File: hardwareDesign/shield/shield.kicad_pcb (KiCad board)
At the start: 2 copper layers, 71 parts, among them J10 PIM_LCD, J11 WQP419, J12 WQP419, J2 40_POS_Header, J3 WQP419, J4 10_POS_PIN_HEADER_ALT, J5 WQP419, J6 WQP419, J7 WQP419, J8 WQP419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

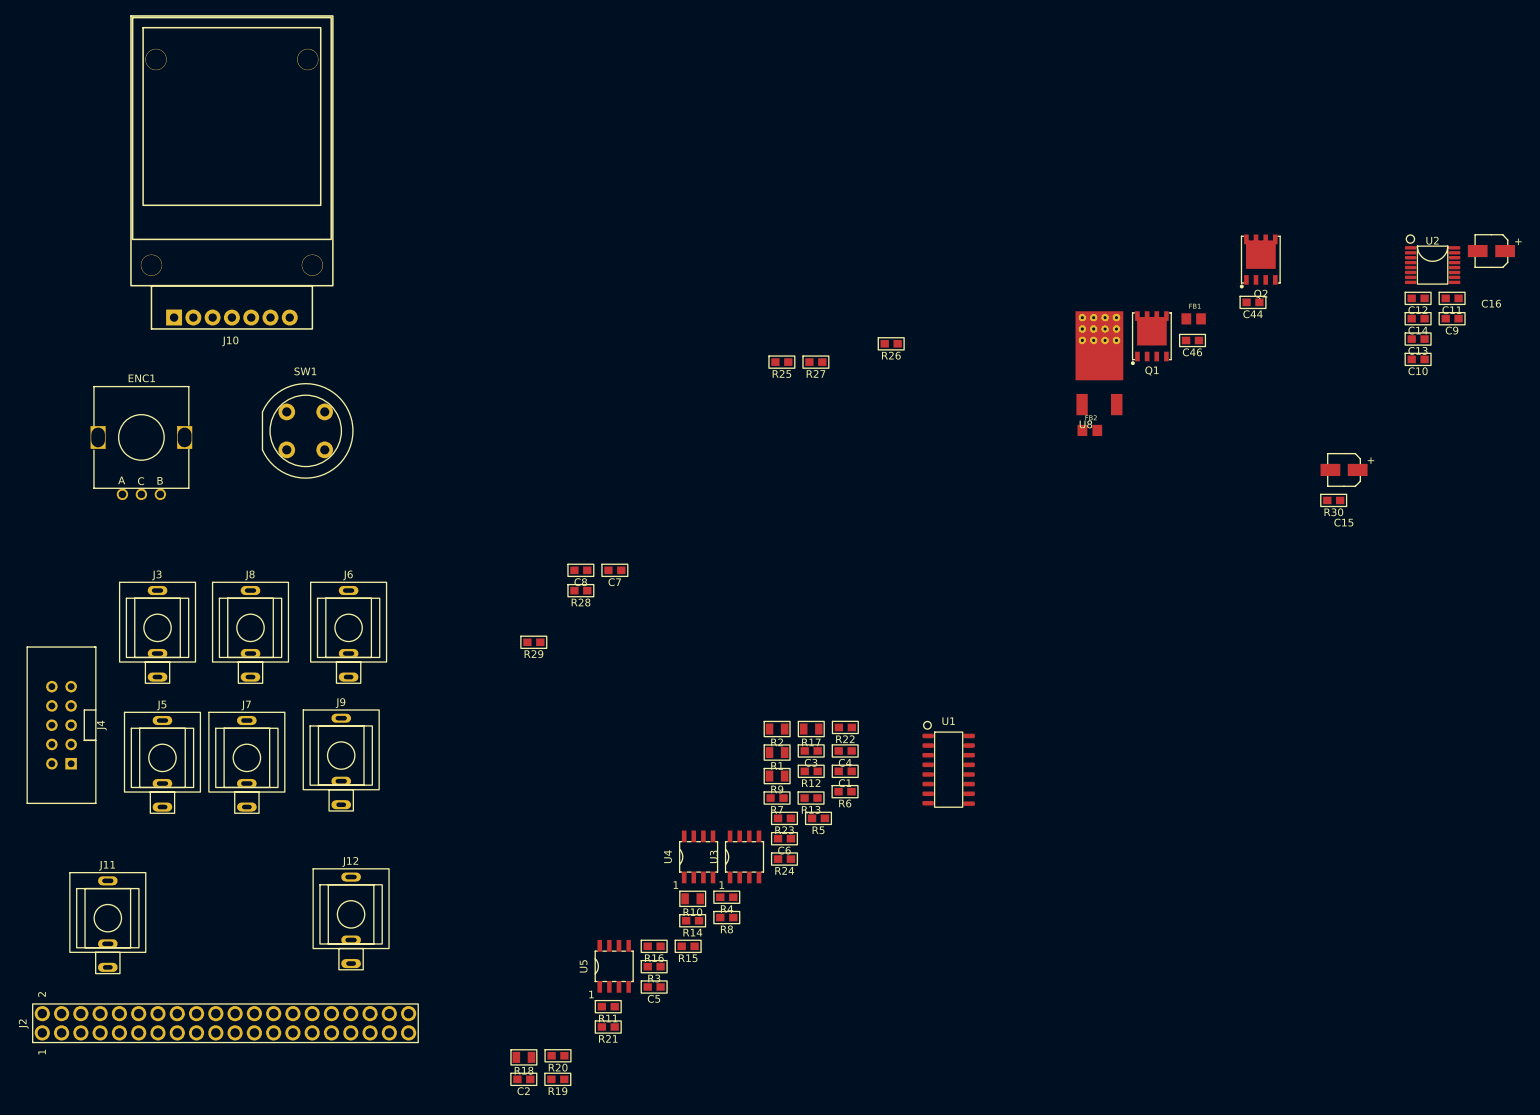
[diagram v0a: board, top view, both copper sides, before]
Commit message: Finished schematic and PCB for jetson Nano Sheild
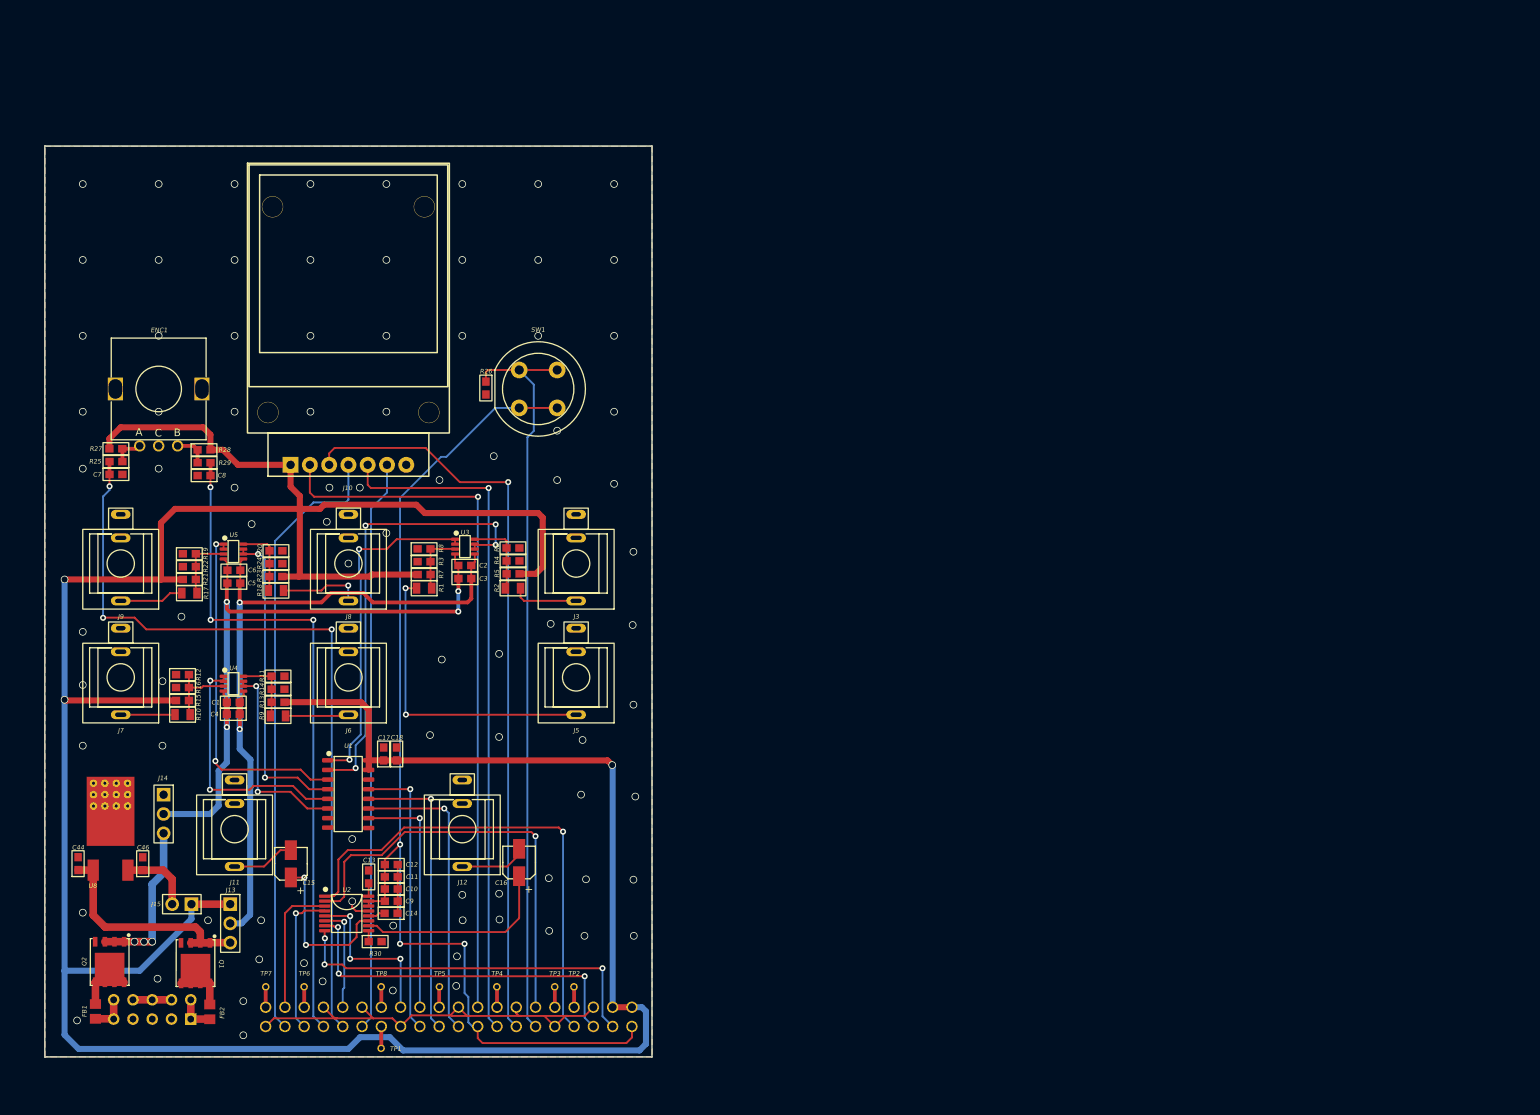
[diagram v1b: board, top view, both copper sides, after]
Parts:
- added C17: 10uf_0603_25V, capacitors:SMD_0603[1608], F.Cu at (64.6, 120.1)
- added C18: 0.1uf_0603_10V, capacitors:SMD_0603[1608], F.Cu at (66.3, 120.1)
- added J13: 3x1_PIN_HEADER, connectors:03x01_2.54_pitch_pin_header, F.Cu at (44.4, 142.4)
- added J14: 3x1_PIN_HEADER, connectors:03x01_2.54_pitch_pin_header, F.Cu at (35.6, 128.0)
- added J15: 2x1_PIN_HEADER, connectors:02x01_2.54_pitch_pin_header, F.Cu at (38.0, 139.9)
- added TP1: test_point_TH_Small, misc:test_point_0.6mm, F.Cu at (64.3, 158.9)
- added TP2: test_point_TH_Small, misc:test_point_0.6mm, F.Cu at (89.7, 150.8)
- added TP3: test_point_TH_Small, misc:test_point_0.6mm, F.Cu at (87.2, 150.8)
- added TP4: test_point_TH_Small, misc:test_point_0.6mm, F.Cu at (79.6, 150.8)
- added TP5: test_point_TH_Small, misc:test_point_0.6mm, F.Cu at (72.0, 150.8)
- added TP6: test_point_TH_Small, misc:test_point_0.6mm, F.Cu at (54.2, 150.8)
- added TP7: test_point_TH_Small, misc:test_point_0.6mm, F.Cu at (49.1, 150.8)
- added TP8: test_point_TH_Small, misc:test_point_0.6mm, F.Cu at (64.3, 150.8)
- J2, J4: moved to B.Cu
- U3, U4, U5: footprint ti:TL072_SOIC-8 -> SOT:SOT23-8
- moved Q2 177.7 mm to (28.5, 147.5), turned to 180 degrees
- moved C44 171.6 mm to (24.4, 134.5), turned to 90 degrees
- moved FB1 171.1 mm to (26.7, 154.0), turned to -90 degrees
- moved U2 166.6 mm to (59.8, 141.1)
- moved C9 159.4 mm to (65.6, 139.5)
- moved C11 159.2 mm to (65.6, 136.3)
- moved C14 156.4 mm to (65.6, 141.1), turned to 180 degrees
- moved C13 155.4 mm to (62.7, 136.3), turned to 90 degrees
- moved C46 154.5 mm to (32.9, 134.6), turned to 90 degrees
- moved C12 154.5 mm to (65.6, 134.7)
- moved C10 152.2 mm to (65.6, 137.9)
- moved C16 151.3 mm to (82.5, 134.4), turned to -90 degrees
- moved Q1 150.7 mm to (39.9, 147.6), turned to 180 degrees
- moved C15 148.1 mm to (52.4, 134.6), turned to -90 degrees
- moved U8 144.0 mm to (28.7, 131.4)
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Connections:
- C1 pad 1: +12V -> /cv_input/OPAMP_VDD
- C1 pad 2: -12V -> /cv_input/OPAMP_VSS
- C2 pad 1: +12V -> /cv_input/OPAMP_VDD
- C2 pad 2: -12V -> /cv_input/OPAMP_VSS
- C3 pad 1: +12V -> /cv_input/OPAMP_VDD
- C3 pad 2: -12V -> /cv_input/OPAMP_VSS
- C4 pad 1: +12V -> /cv_input/OPAMP_VDD
- C4 pad 2: -12V -> /cv_input/OPAMP_VSS
- C46 pad 1: +5V -> Net-(C46-Pad1)
- C5 pad 1: +12V -> /cv_input/OPAMP_VDD
- C5 pad 2: -12V -> /cv_input/OPAMP_VSS
- C6 pad 1: +12V -> /cv_input/OPAMP_VDD
- C6 pad 2: -12V -> /cv_input/OPAMP_VSS
- J2 pad 10: unconnected-(J2-Pad10) -> Net-(J2-Pad10)
- J2 pad 16: unconnected-(J2-Pad16) -> Net-(J2-Pad16)
- J2 pad 22: unconnected-(J2-Pad22) -> Net-(J2-Pad22)
- J2 pad 27: unconnected-(J2-Pad27) -> Net-(J2-Pad27)
- J2 pad 28: unconnected-(J2-Pad28) -> Net-(J2-Pad28)
- J2 pad 36: unconnected-(J2-Pad36) -> Net-(J2-Pad36)
- J2 pad 40: unconnected-(J2-Pad40) -> Net-(J2-Pad40)
- J2 pad 8: unconnected-(J2-Pad8) -> Net-(J2-Pad8)
- U3 pad 4: -12V -> /cv_input/OPAMP_VSS
- U3 pad 8: +12V -> /cv_input/OPAMP_VDD
- U4 pad 4: -12V -> /cv_input/OPAMP_VSS
- U4 pad 8: +12V -> /cv_input/OPAMP_VDD
- U5 pad 4: -12V -> /cv_input/OPAMP_VSS
- U5 pad 8: +12V -> /cv_input/OPAMP_VDD
- U8 pad 3: +5V -> Net-(C46-Pad1)
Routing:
- net +5V: track 0.00 -> 420.3 mm, vias 0 -> 3
- net +3V3: track 0.00 -> 140.6 mm, vias 0 -> 3
- net /GPIO_200: track 0.00 -> 104.6 mm, vias 0 -> 3
- net /SPI_2_SCK: track 0.00 -> 99.4 mm, vias 0 -> 1
- net /GPIO_50: track 0.00 -> 98.9 mm
- net /cv_input/OPAMP_VDD: track 0.00 -> 93.9 mm, vias 0 -> 2
- net /SPI_2_CS0: track 0.00 -> 93.3 mm, vias 0 -> 1
- net /GPIO_194: track 0.00 -> 90.1 mm, vias 0 -> 1
- net /GPIO_38: track 0.00 -> 88.4 mm, vias 0 -> 3
- net /cv_input/OPAMP_VSS: track 0.00 -> 85.2 mm, vias 0 -> 4
- net /SPI_2_MOSI: track 0.00 -> 81.0 mm
- net /GPIO_149: track 0.00 -> 75.4 mm
- net GND: track 0.00 -> 73.6 mm, vias 0 -> 87
- net /AUDIO_MCLK: track 0.00 -> 64.1 mm, vias 0 -> 1
- net /adc/ADC_IN1: track 0.00 -> 59.7 mm, vias 0 -> 4
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- added copper zone on B.Cu, net GND
- added copper zone on F.Cu, net GND
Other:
- board outline added: 80 x 120 mm
- board text added: "Jetson Nano"
- board text added: "Position: X = 20, Y = 40"

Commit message: Finished layout with JN real footprint
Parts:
- added JN1: JetsonNano, singleBoardComp:jetsonNanoDev, B.Cu at (82.5, 44.5)
- TP1, TP2, TP3, TP4, TP5, TP6, TP7, TP8: moved to B.Cu
- moved C44 71.7 mm to (96.0, 132.6), turned to -90 degrees
- moved U8 63.2 mm to (91.7, 135.7), turned to 180 degrees
- moved C46 54.6 mm to (87.5, 132.6), turned to -90 degrees
- moved FB2 54.5 mm to (96.3, 155.0)
- moved J4 54.5 mm to (88.7, 154.7)
- moved FB1 54.5 mm to (81.2, 154.9)
- moved Q1 54.5 mm to (94.4, 148.6)
- moved Q2 54.5 mm to (83.1, 148.4)
- moved J13 52.4 mm to (93.5, 124.0), turned to 0 degrees
- moved J14 51.6 mm to (87.2, 125.8)
- moved J15 37.0 mm to (74.8, 143.9), turned to 0 degrees
- moved C14 30.9 mm to (35.2, 135.7)
- moved C9 30.9 mm to (35.2, 134.1)
- moved R30 30.9 mm to (33.1, 139.4)
- moved U2 30.9 mm to (29.4, 135.7)
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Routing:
- net +5V: track 420.3 -> 300.1 mm, vias 3 -> 10
- net GND: track 73.6 -> 25.5 mm, vias 87 -> 132
- net +3V3: track 140.6 -> 180.2 mm, vias 3 -> 2
- net /I2C_2_SCL: track 47.6 -> 72.2 mm, vias 3 -> 1
- net /SPI_2_SCK: track 99.4 -> 75.3 mm, vias 1 -> 0
- net /GPIO_149: track 75.4 -> 99.4 mm, vias 0 -> 2
- net /I2S_4_SCLK: track 57.0 -> 80.4 mm
- net /I2C_2_SDA: track 49.5 -> 72.1 mm, vias 3 -> 1
- net /GPIO_19: track 22.0 -> 44.5 mm, vias 3 -> 1
- net /GPIO_168: track 14.0 -> 35.7 mm
- net /SPI_2_CS0: track 93.3 -> 71.7 mm, vias 1 -> 0
- net /SPI_2_MOSI: track 81.0 -> 101.0 mm, vias 0 -> 2
- net /GPIO_200: track 104.6 -> 85.3 mm, vias 3 -> 1
- net /AUDIO_MCLK: track 64.1 -> 83.5 mm
- net /cv_input/OPAMP_VSS: track 85.2 -> 103.5 mm, vias 4 -> 5
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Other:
- board text removed: "Jetson Nano"
